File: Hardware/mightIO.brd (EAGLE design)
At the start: 37.8 x 31.7 mm, 45 parts, among them IC1 TL064D, IC2 TL064D, IC3 LM4041A12DBZ, U1 MAX11612

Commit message: Some part value updates
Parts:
- C11, C13: value 47pF -> 220pF
- C12, C9: value 220pF -> 47pF
- C4, C5, C6, C7: value 1uF -> 2.2uF
- R10, R11, R14, R5: value 100k -> 20k
- R12, R13, R6, R9: value 20k -> 100k
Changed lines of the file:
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@@
 <element name="C2" library="rcl" package="C0603" value="0.1uF" x="23.1775" y="8.255" rot="MR270"/>
 <element name="C3" library="rcl" package="C0603" value="0.1uF" x="19.05" y="8.255" rot="R90"/>
-<element name="C4" library="rcl" package="C0603" value="1uF" x="13.97" y="14.9225" rot="R180"/>
-<element name="C5" library="rcl" package="C0603" value="1uF" x="9.2075" y="11.7475" rot="R270"/>
-<element name="C7" library="rcl" package="C0603" value="1uF" x="19.05" y="11.43" rot="R270"/>
-<element name="C6" library="rcl" package="C0603" value="1uF" x="16.51" y="11.7475" rot="MR270"/>
+<element name="C4" library="rcl" package="C0603" value="2.2uF" x="13.97" y="14.9225" rot="R180"/>
+<element name="C5" library="rcl" package="C0603" value="2.2uF" x="9.2075" y="11.7475" rot="R270"/>
+<element name="C7" library="rcl" package="C0603" value="2.2uF" x="19.05" y="11.43" rot="R270"/>
+<element name="C6" library="rcl" package="C0603" value="2.2uF" x="16.51" y="11.7475" rot="MR270"/>
 <element name="IC1" library="linear" package="SO14" value="TL064D" x="18.415" y="21.59" rot="R270"/>
 <element name="IC2" library="linear" package="SO14" value="TL064D" x="18.415" y="21.59" rot="MR90"/>
@@
 <element name="R4" library="rcl" package="R0603" value="20k" x="10.4775" y="24.765" rot="R270"/>
 <element name="C8" library="rcl" package="C0603" value="220pF" x="12.7" y="24.765" rot="R90"/>
-<element name="R5" library="rcl" package="R0603" value="100k" x="27.6225" y="13.97" rot="MR270"/>
-<element name="R6" library="rcl" package="R0603" value="20k" x="26.3525" y="24.765" rot="R270"/>
-<element name="C9" library="rcl" package="C0603" value="220pF" x="24.13" y="24.765" rot="R90"/>
+<element name="R5" library="rcl" package="R0603" value="20k" x="27.6225" y="13.97" rot="MR270"/>
+<element name="R6" library="rcl" package="R0603" value="100k" x="26.3525" y="24.765" rot="R270"/>
+<element name="C9" library="rcl" package="C0603" value="47pF" x="24.13" y="24.765" rot="R90"/>
 <element name="R7" library="rcl" package="R0603" value="20k" x="23.1775" y="13.97" rot="MR270"/>
 <element name="R8" library="rcl" package="R0603" value="100k" x="26.3525" y="18.415" rot="MR90"/>
 <element name="C10" library="rcl" package="C0603" value="47pF" x="24.13" y="18.415" rot="MR270"/>
-<element name="R9" library="rcl" package="R0603" value="20k" x="6.6675" y="22.86" rot="R180"/>
-<element name="R10" library="rcl" package="R0603" value="100k" x="10.4775" y="24.765" rot="MR270"/>
-<element name="C11" library="rcl" package="C0603" value="47pF" x="12.7" y="24.765" rot="MR90"/>
-<element name="R11" library="rcl" package="R0603" value="100k" x="25.4" y="13.97" rot="MR270"/>
-<element name="R12" library="rcl" package="R0603" value="20k" x="26.3525" y="18.415" rot="R90"/>
-<element name="C12" library="rcl" package="C0603" value="220pF" x="24.13" y="18.415" rot="R270"/>
-<element name="R13" library="rcl" package="R0603" value="20k" x="6.6675" y="20.32" rot="R180"/>
-<element name="R14" library="rcl" package="R0603" value="100k" x="12.7" y="18.415" rot="MR90"/>
-<element name="C13" library="rcl" package="C0603" value="47pF" x="10.4775" y="18.415" rot="MR270"/>
+<element name="R9" library="rcl" package="R0603" value="100k" x="6.6675" y="22.86" rot="R180"/>
+<element name="R10" library="rcl" package="R0603" value="20k" x="10.4775" y="24.765" rot="MR270"/>
+<element name="C11" library="rcl" package="C0603" value="220pF" x="12.7" y="24.765" rot="MR90"/>
+<element name="R11" library="rcl" package="R0603" value="20k" x="25.4" y="13.97" rot="MR270"/>
+<element name="R12" library="rcl" package="R0603" value="100k" x="26.3525" y="18.415" rot="R90"/>
+<element name="C12" library="rcl" package="C0603" value="47pF" x="24.13" y="18.415" rot="R270"/>
+<element name="R13" library="rcl" package="R0603" value="100k" x="6.6675" y="20.32" rot="R180"/>
+<element name="R14" library="rcl" package="R0603" value="20k" x="12.7" y="18.415" rot="MR90"/>
+<element name="C13" library="rcl" package="C0603" value="220pF" x="10.4775" y="18.415" rot="MR270"/>
 <element name="R17" library="rcl" package="R0603" value="100k" x="6.6675" y="18.0975" rot="R180"/>
 <element name="R18" library="rcl" package="R0603" value="20k" x="10.4775" y="18.415" rot="R90"/>

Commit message: Some routing updates, more needed
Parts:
- added C14: 0.1uF, rcl:C0603
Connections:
- net GND: now also C14.1
- net VREF: now also C14.2
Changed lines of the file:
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@@
 <?xml version="1.0" encoding="utf-8"?>
 <!DOCTYPE eagle SYSTEM "eagle.dtd">
-<eagle version="6.5.0">
+<eagle version="7.0.0">
 <drawing>
 <settings>
@@
 <layer number="37" name="tTest" color="7" fill="1" visible="no" active="yes"/>
 <layer number="38" name="bTest" color="7" fill="1" visible="no" active="yes"/>
-<layer number="39" name="tKeepout" color="4" fill="11" visible="yes" active="yes"/>
-<layer number="40" name="bKeepout" color="1" fill="11" visible="yes" active="yes"/>
-<layer number="41" name="tRestrict" color="4" fill="10" visible="yes" active="yes"/>
-<layer number="42" name="bRestrict" color="1" fill="10" visible="yes" active="yes"/>
-<layer number="43" name="vRestrict" color="2" fill="10" visible="yes" active="yes"/>
+<layer number="39" name="tKeepout" color="4" fill="11" visible="no" active="yes"/>
+<layer number="40" name="bKeepout" color="1" fill="11" visible="no" active="yes"/>
+<layer number="41" name="tRestrict" color="4" fill="10" visible="no" active="yes"/>
+<layer number="42" name="bRestrict" color="1" fill="10" visible="no" active="yes"/>
+<layer number="43" name="vRestrict" color="2" fill="10" visible="no" active="yes"/>
 <layer number="44" name="Drills" color="7" fill="1" visible="no" active="yes"/>
 <layer number="45" name="Holes" color="7" fill="1" visible="no" active="yes"/>
 <layer number="46" name="Milling" color="3" fill="1" visible="no" active="yes"/>
 <layer number="47" name="Measures" color="7" fill="1" visible="no" active="yes"/>
-<layer number="48" name="Document" color="7" fill="1" visible="yes" active="yes"/>
-<layer number="49" name="Reference" color="7" fill="1" visible="yes" active="yes"/>
-<layer number="51" name="tDocu" color="7" fill="1" visible="yes" active="yes"/>
-<layer number="52" name="bDocu" color="7" fill="1" visible="yes" active="yes"/>
+<layer number="48" name="Document" color="7" fill="1" visible="no" active="yes"/>
+<layer number="49" name="Reference" color="7" fill="1" visible="no" active="yes"/>
+<layer number="51" name="tDocu" color="7" fill="1" visible="no" active="yes"/>
+<layer number="52" name="bDocu" color="7" fill="1" visible="no" active="yes"/>
 <layer number="91" name="Nets" color="2" fill="1" visible="no" active="no"/>
 <layer number="92" name="Busses" color="1" fill="1" visible="no" active="no"/>
@@
 <pass name="Default">
 <param name="RoutingGrid" value="50mil"/>
+<param name="AutoGrid" value="1"/>
+<param name="Efforts" value="0"/>
+<param name="TopRouterVariant" value="1"/>
 <param name="tpViaShape" value="round"/>
 <param name="PrefDir.1" value="|"/>
@@
 <element name="JP3" library="pinhead" package="1X04" value="Banana" x="3.175" y="21.59" rot="R90"/>
 <element name="JP4" library="pinhead" package="1X04" value="Mango" x="32.385" y="21.59" rot="R90"/>
+<element name="C14" library="rcl" package="C0603" value="0.1uF" x="22.225" y="13.97" rot="R90"/>
 </elements>
 <signals>
@@
 <via x="35.8775" y="1.905" extent="1-16" drill="0.6" shape="square"/>
 <via x="1.905" y="1.905" extent="1-16" drill="0.6" shape="square"/>
+<contactref element="C14" pad="1"/>
 </signal>
 <signal name="+5V" class="1">
@@
 <wire x1="5.295" y1="9.945" x2="5.3975" y2="9.8425" width="0.4064" layer="16"/>
 <via x="5.3975" y="9.8425" extent="1-16" drill="0.6" shape="square"/>
-<wire x1="5.3975" y1="9.8425" x2="11.315" y2="9.8425" width="0.4064" layer="1"/>
+<wire x1="11.315" y1="9.8425" x2="5.3975" y2="9.8425" width="0.4064" layer="1"/>
 <wire x1="13.335" y1="5.715" x2="13.335" y2="5.08" width="0.4064" layer="1"/>
 <wire x1="23.1775" y1="7.405" x2="23.3925" y2="7.62" width="0.3048" layer="16"/>
@@
 <wire x1="15.815" y1="22.86" x2="13.97" y2="22.86" width="0.4064" layer="1"/>
 <wire x1="13.97" y1="22.86" x2="13.97" y2="21.59" width="0.4064" layer="1"/>
+<contactref element="C14" pad="2"/>
+<wire x1="22.225" y1="14.82" x2="20.955" y2="15.24" width="0" layer="19" extent="1-1"/>
 </signal>
 <signal name="SDA">

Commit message: Layout tweaks, added cap
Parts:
- added C17: 10uF, rcl:E2,5-6
- moved C2 6.35 mm to (29.5, 8.26)
- moved IC3 4.45 mm to (28.3, 11.1)
- moved R15 3.81 mm to (24.1, 11.4)
- moved R21 2.62 mm to (28.6, 13.3)
- moved R16 2.54 mm to (25.7, 13.3)
- moved C3 0.63 mm to (19.1, 8.89)
- moved C4 0.63 mm to (14.0, 15.6)
- moved C5 0.63 mm to (9.21, 12.4)
- moved C6 0.63 mm to (16.5, 12.4)
- moved C7 0.63 mm to (19.1, 12.1)
- moved U$1 0.63 mm to (14.0, 11.4)
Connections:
- net +5V: now also C17.+
- net GND: now also C17.-
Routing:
- net +5V: track 69.1 -> 83.9 mm, vias 4 -> 3
- net VREF: track 47.5 -> 44.7 mm
- net N$26: track 5.40 -> 4.39 mm
- net N$13: track 3.41 -> 2.75 mm
- net V+: track 16.2 -> 15.6 mm
- net V-: track 22.0 -> 21.4 mm

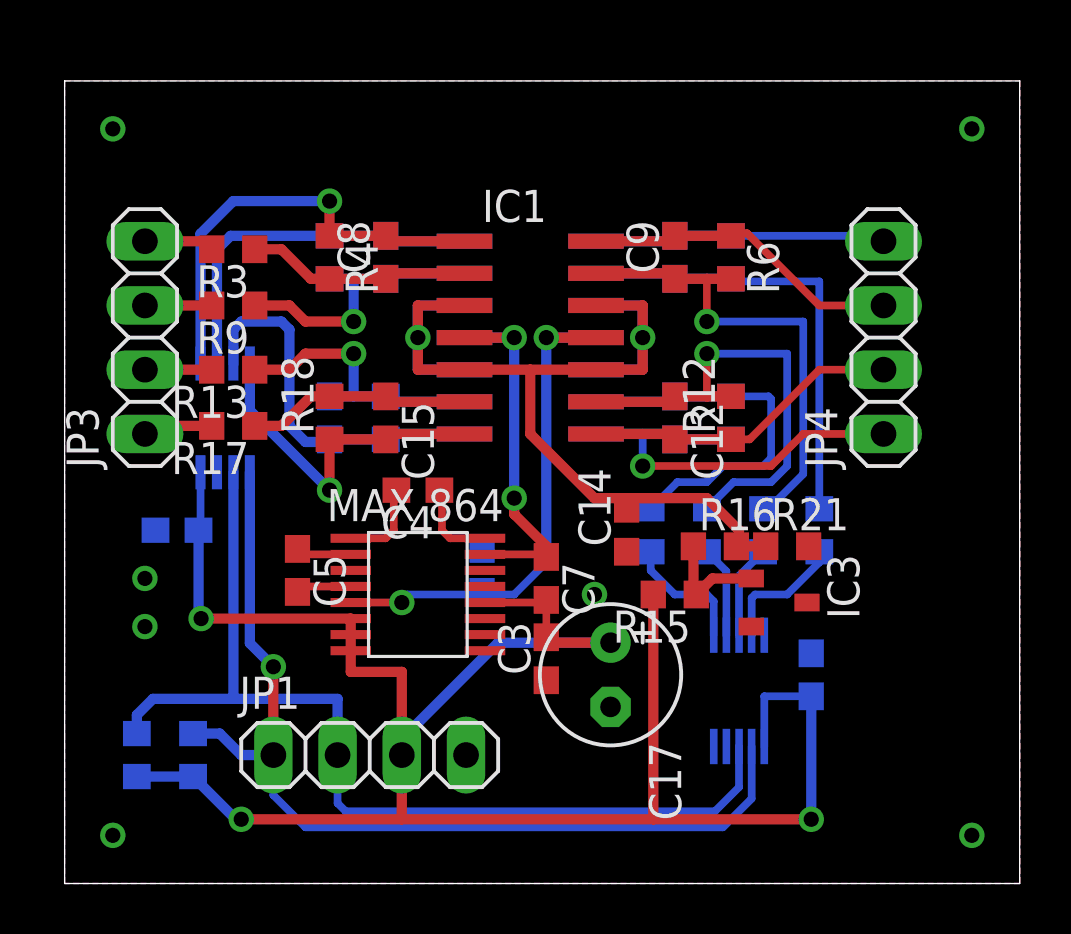
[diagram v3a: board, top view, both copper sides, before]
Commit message: Added silkscreen, ready to go
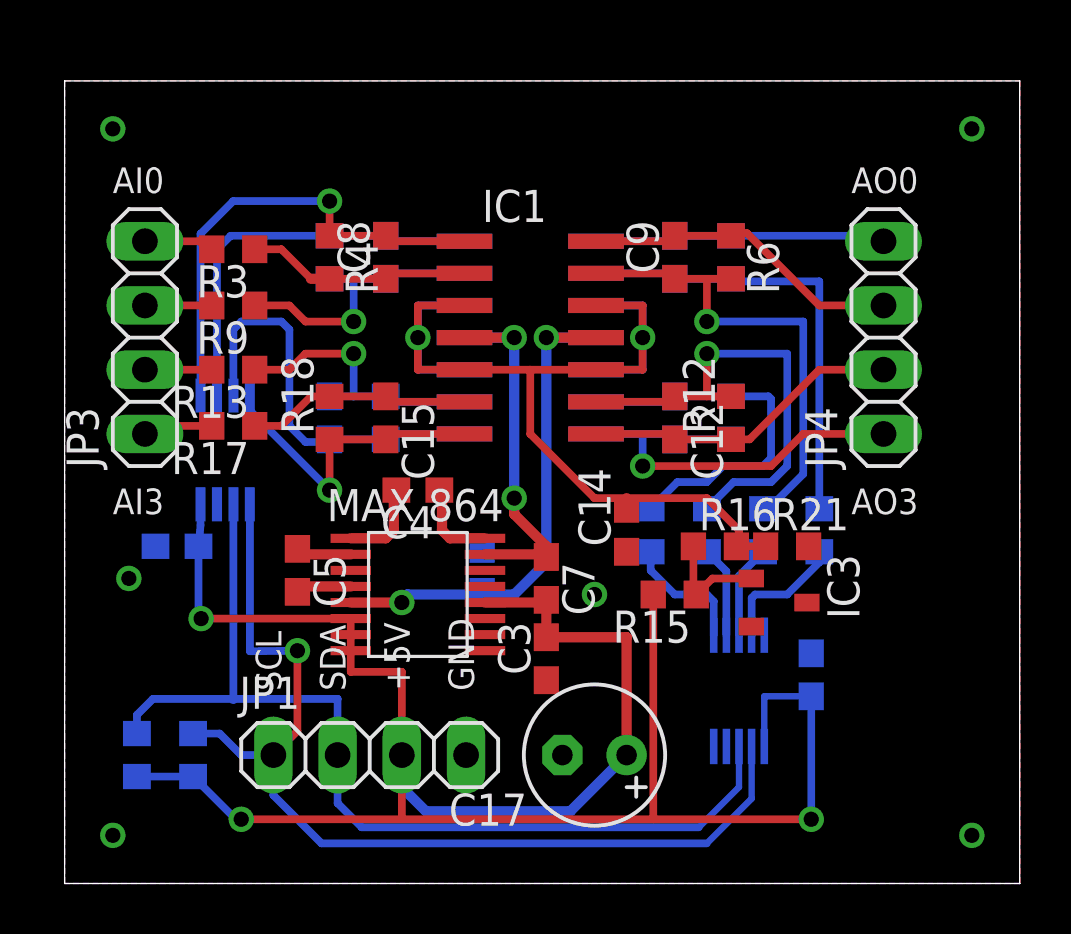
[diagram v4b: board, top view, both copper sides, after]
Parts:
- moved C17 3.24 mm to (21.0, 5.08), turned to 180 degrees
- moved U1 1.27 mm to (6.35, 17.1)
- moved C1 0.63 mm to (4.45, 13.3)
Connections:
- net N$13 renamed AI0
- net N$14 renamed AOB
- net N$16 renamed AI2
- net N$2 renamed AOD
- net N$24 renamed AOA
- net N$30 renamed AOC
- net N$5 renamed AI1
- net N$6 renamed AI3
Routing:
- net +5V: track 83.9 -> 89.5 mm
- net N$12: track 15.0 -> 16.2 mm
- net N$22: track 13.7 -> 12.5 mm
- net N$20: track 14.6 -> 15.9 mm
- net N$18: track 18.0 -> 19.2 mm
- net SCL: track 38.7 -> 39.8 mm
- net SDA: track 40.0 -> 39.3 mm
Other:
- board text added: "+5V"
- board text added: "AI0"
- board text added: "AI3"
- board text added: "AO0"
- board text added: "AO3"
- board text added: "GND"
- board text added: "SCL"
- board text added: "SDA"

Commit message: Gerber files done
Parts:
- moved C10 1.14 mm to (25.1, 19.1)
- moved C12 1.14 mm to (25.1, 19.1)
- moved C13 1.14 mm to (11.4, 19.1)
- moved C15 1.14 mm to (13.7, 19.1)
- moved IC1 1.14 mm to (19.4, 22.2)
- moved IC2 1.14 mm to (19.4, 22.2)
- moved JP3 1.14 mm to (4.13, 22.2)
- moved JP4 1.14 mm to (33.3, 22.2)
- moved R12 1.14 mm to (27.3, 19.1)
- moved R14 1.14 mm to (13.7, 19.1)
- moved R18 1.14 mm to (11.4, 19.1)
- moved R8 1.14 mm to (27.3, 19.1)
- moved U1 1.14 mm to (7.30, 17.8)
- moved C17 1.14 mm to (21.9, 5.71)
- moved C2 1.14 mm to (30.5, 8.89)
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
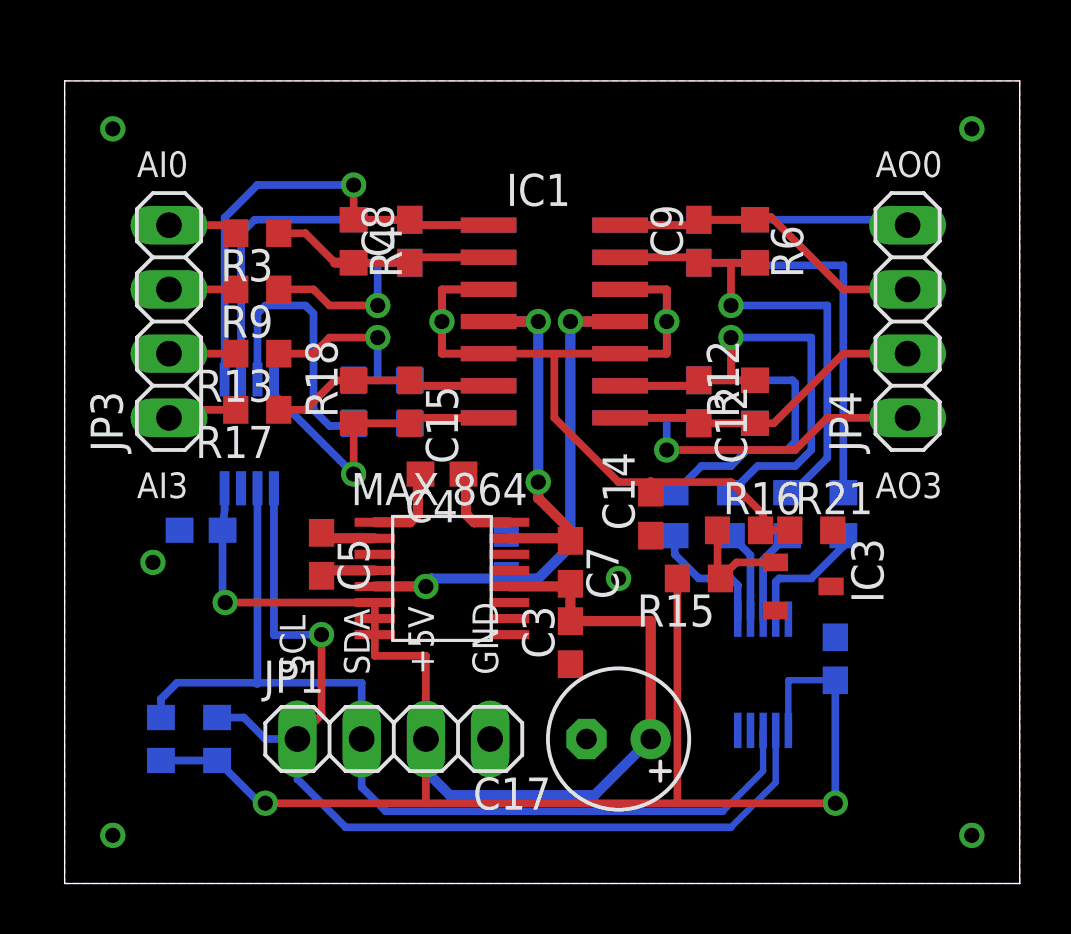
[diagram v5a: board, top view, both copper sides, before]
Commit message: Switched output amplifiers to non-inverting
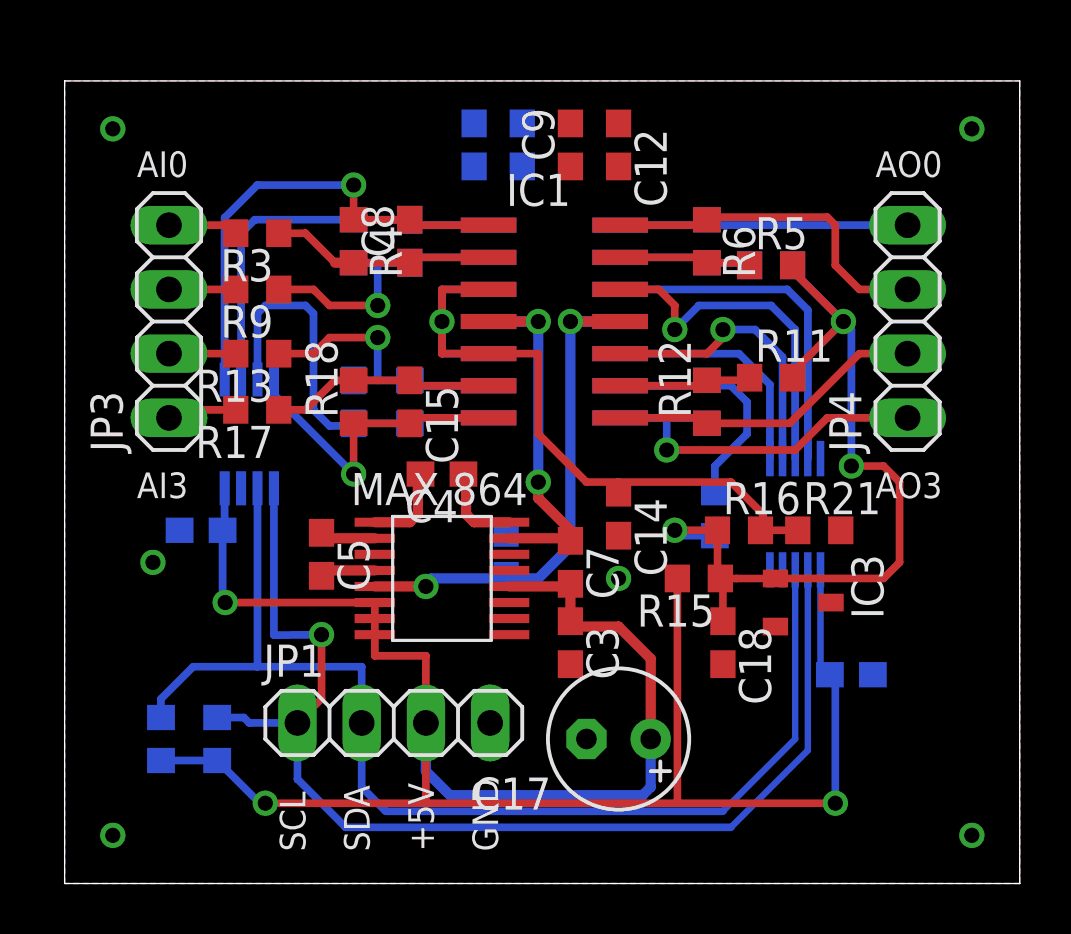
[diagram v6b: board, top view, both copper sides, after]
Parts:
- added C18: 0.1uF, rcl:C0603
- JP1: value Apple -> (none)
- JP3: value Banana -> (none)
- JP4: value Mango -> (none)
- R11, R19, R5, R7: value 20k -> 22k
- R16: value 2k -> 1k
- R21: value 10k -> 5.1k
- moved C10 13.5 mm to (16.2, 29.2)
- moved C12 10.6 mm to (21.9, 29.2)
- moved R19 10.2 mm to (27.9, 24.4), turned to 180 degrees
- moved R5 9.86 mm to (27.9, 24.4), flipped to the top, turned to 0 degrees
- moved C16 7.96 mm to (18.1, 29.2)
- moved U$2 6.48 mm to (28.9, 14.6)
- moved C9 6.35 mm to (20.0, 29.2)
- moved R11 5.63 mm to (27.9, 20.0), flipped to the top, turned to 0 degrees
- moved R12 1.91 mm to (25.4, 19.1)
- moved R20 1.91 mm to (25.4, 25.4)
- moved R6 1.91 mm to (25.4, 25.4)
- moved R8 1.91 mm to (25.4, 19.1)
- moved R7 1.59 mm to (25.7, 14.6)
- moved C14 1.27 mm to (21.9, 14.6), turned to 270 degrees
- moved C2 0.90 mm to (31.1, 8.26), turned to 180 degrees
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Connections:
- removed net N$15: C9.1, IC1.13, R5.1, R6.2
- removed net N$17: C10.1, IC2.13, R7.1, R8.2
- removed net N$21: C12.1, IC1.9, R11.1, R12.2
- removed net N$26: IC3.1, R15.1, R16.1
- removed net N$29: C16.1, IC2.9, R19.1, R20.2
- removed net VREF: C14.2, IC1.10, IC1.12, IC1.3, IC1.5, IC2.10, IC2.12, IC2.3, IC2.5, R16.2, R21.1
- new net N$2: IC2.9, R19.1, R20.2
- new net N$4: IC1.13, R5.1, R6.2
- new net N$5: IC1.9, R11.1, R12.2
- new net N$6: IC2.13, R7.1, R8.2
- new net VREFIN: C14.1, IC1.3, IC1.5, IC2.3, IC2.5, R16.2, R21.1
- new net VREFOUT: C18.1, IC3.1, R11.2, R15.1, R16.1, R19.2, R5.2, R7.2
- net +5V: now also C1.1, C2.1, C3.1; no longer C1.2, C2.2, C3.2
- net AOA: no longer C10.2
- net AOB: no longer C12.2
- net AOC: no longer C9.2
- net AOD: no longer C16.2
- net GND: now also C1.2, C14.2, C18.2, C2.2, C3.2; no longer C1.1, C14.1, C2.1, C3.1
- net N$1: now also IC2.10; no longer R19.2
- net N$25: now also IC2.12; no longer R7.2
- net N$3: now also IC1.10; no longer R11.2
- net N$34: now also IC1.12; no longer R5.2
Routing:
- net VREF: track 44.7 -> 0.00 mm, vias 2 -> 0
- net VREFOUT: track 0.00 -> 34.8 mm, vias 0 -> 3
- net VREFIN: track 0.00 -> 30.4 mm, vias 0 -> 1
- net N$15: track 19.1 -> 0.00 mm, vias 1 -> 0
- net N$21: track 18.6 -> 0.00 mm, vias 1 -> 0
- net N$29: track 18.0 -> 0.00 mm
- net N$17: track 15.0 -> 0.00 mm
- net N$34: track 3.69 -> 14.0 mm, vias 0 -> 1
- net N$6: track 0.00 -> 9.62 mm
- net N$1: track 5.15 -> 13.6 mm
- net N$3: track 3.62 -> 11.5 mm, vias 0 -> 1
- net SDA: track 39.3 -> 46.4 mm
- net SCL: track 39.8 -> 46.4 mm
- net N$4: track 0.00 -> 5.79 mm
- net N$2: track 0.00 -> 5.79 mm
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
